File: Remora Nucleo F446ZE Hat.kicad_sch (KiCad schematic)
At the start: 20 parts, among them J1 NucleoF446ZE CN11 Header, J2 MSD-1-A, J3 UART_TX, J4 NucleoF446ZE CN12 Header, SW1 SW_Push

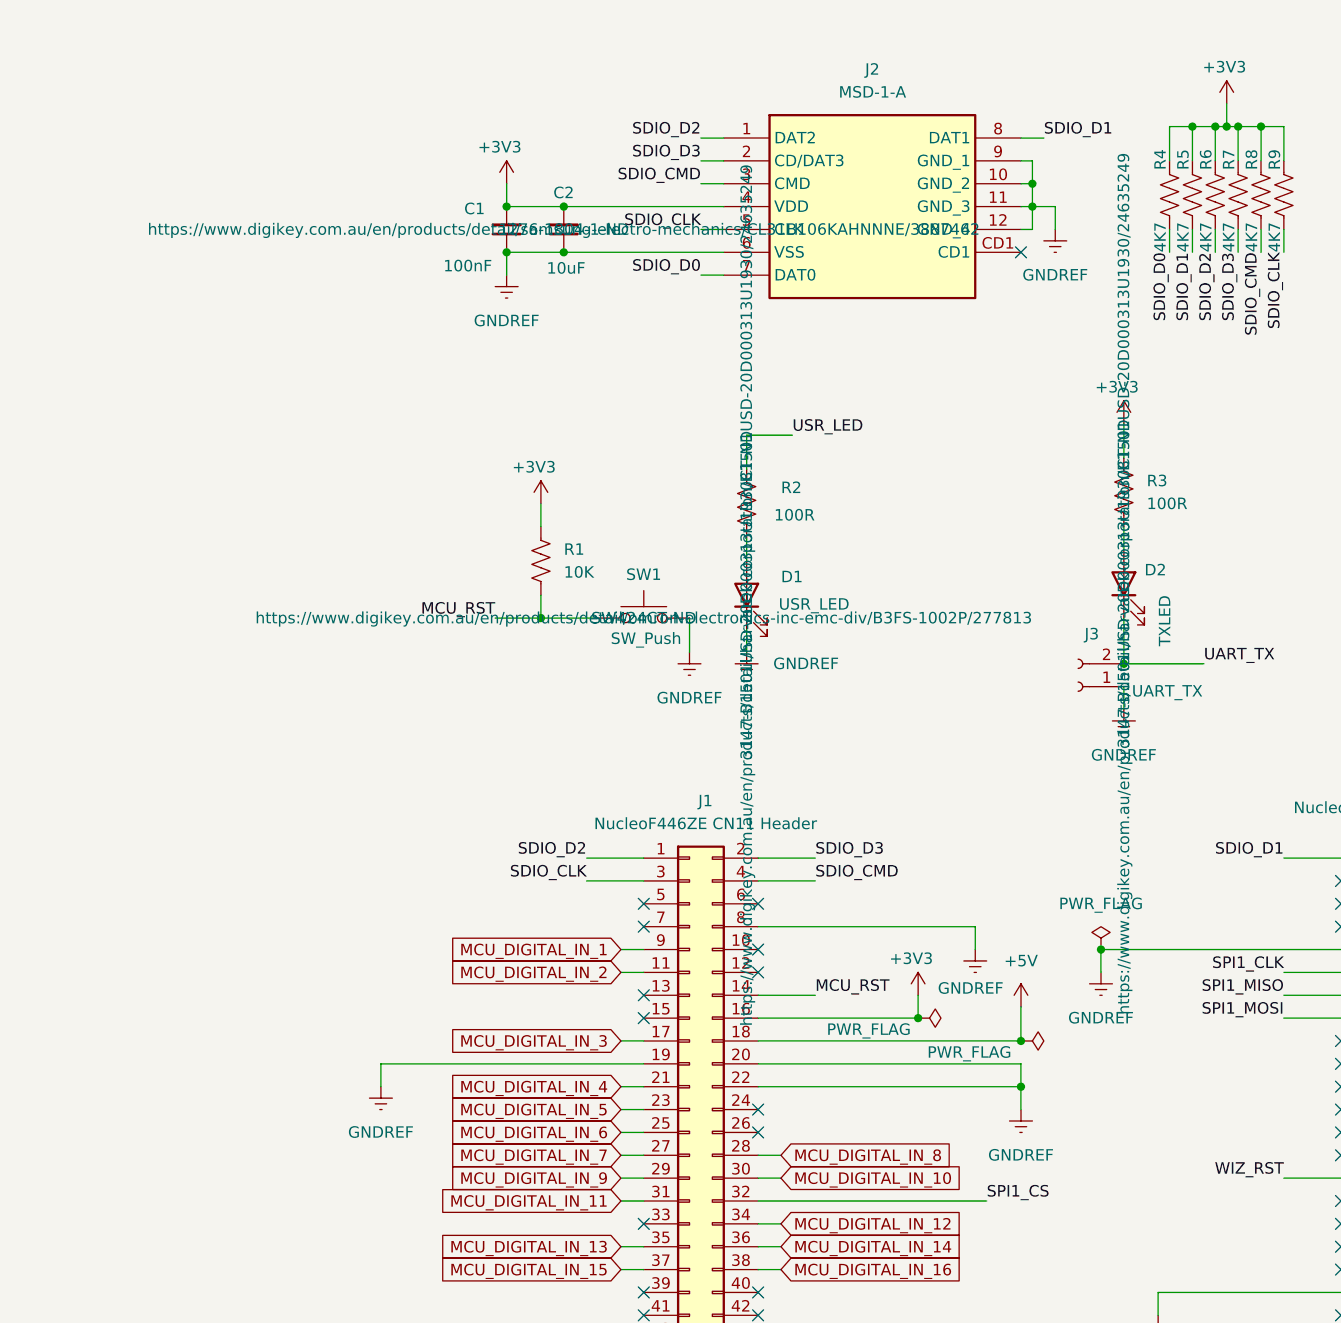
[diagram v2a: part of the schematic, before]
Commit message: fix to annoying additional symbol fields displaying when we didn't want them to.
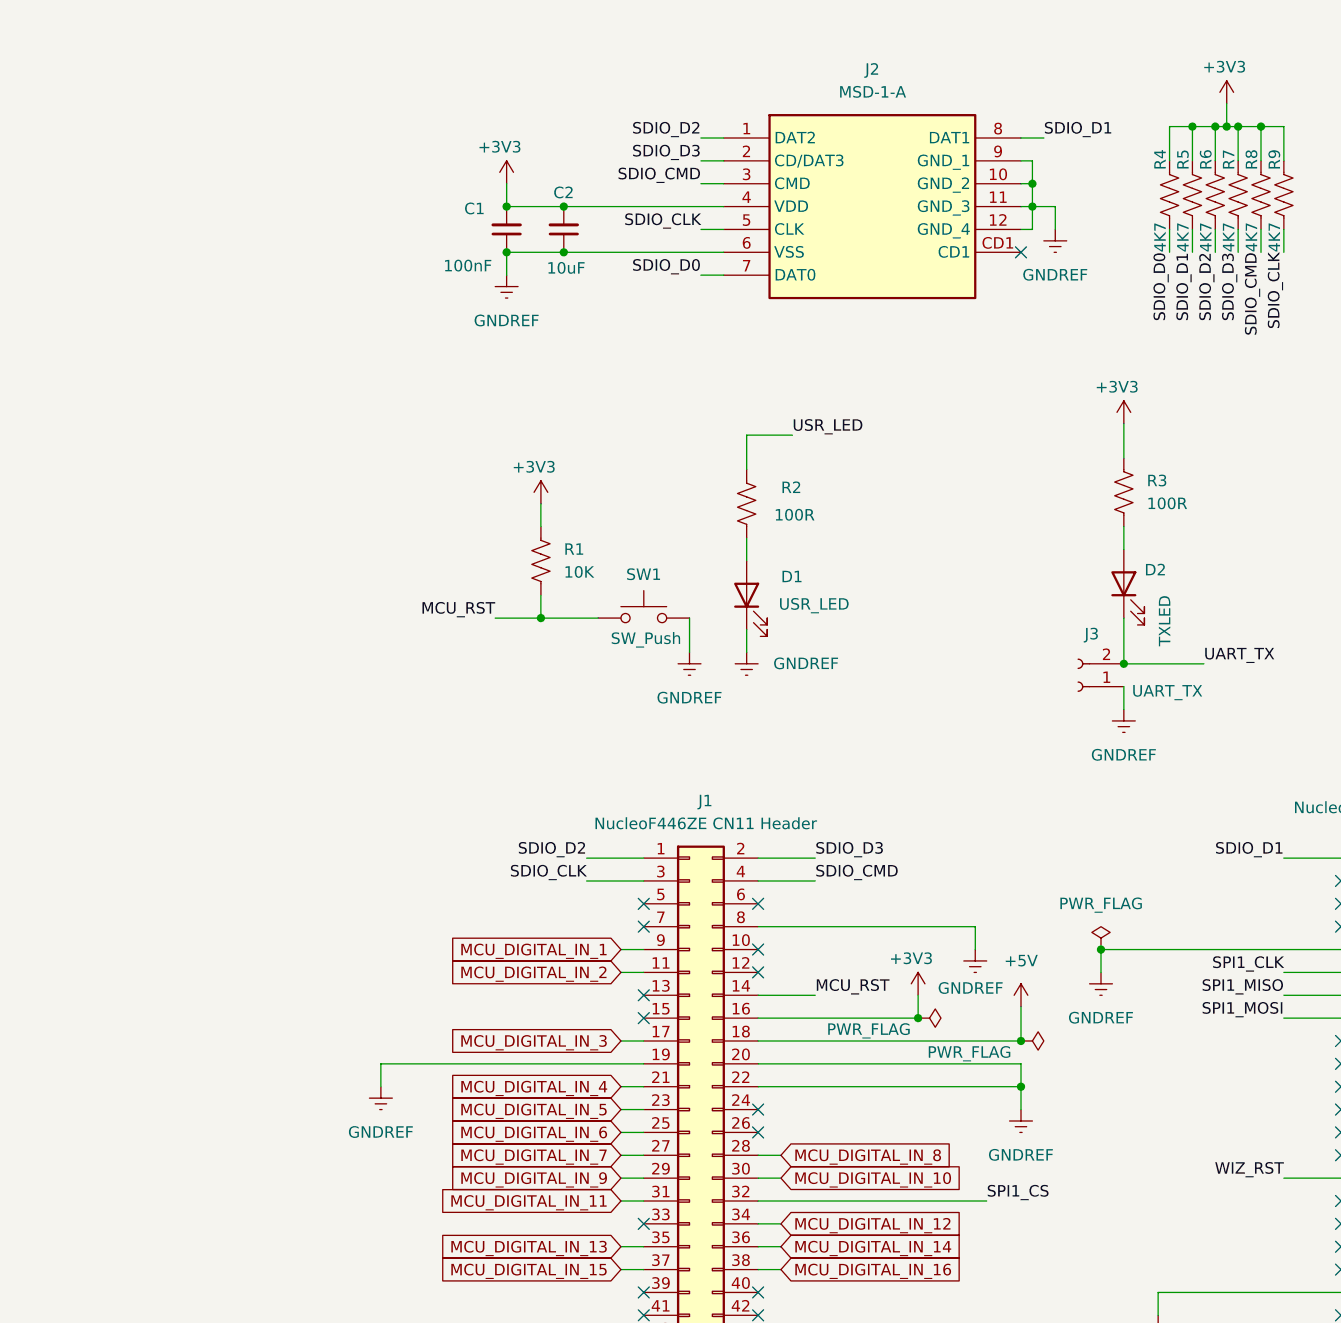
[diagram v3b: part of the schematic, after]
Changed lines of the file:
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@@
 					(size 1.27 1.27)
 				)
+				(hide yes)
 			)
 		)
@@
 					(size 1.27 1.27)
 				)
+				(hide yes)
 			)
 		)
@@
 					(size 1.27 1.27)
 				)
+				(hide yes)
 			)
 		)
@@
 					(size 1.27 1.27)
 				)
+				(hide yes)
 			)
 		)
@@
 					(size 1.27 1.27)
 				)
+				(hide yes)
 			)
 		)
@@
 					(size 1.27 1.27)
 				)
+				(hide yes)
 			)
 		)
@@
 					(size 1.27 1.27)
 				)
+				(hide yes)
 			)
 		)
@@
 					(size 1.27 1.27)
 				)
+				(hide yes)
 			)
 		)
@@
 					(size 1.27 1.27)
 				)
+				(hide yes)
 			)
 		)
@@
 					(size 1.27 1.27)
 				)
+				(hide yes)
 			)
 		)
@@
 					(size 1.27 1.27)
 				)
+				(hide yes)
 			)
 		)
@@
 					(size 1.27 1.27)
 				)
+				(hide yes)
 			)
 		)
@@
 					(size 1.27 1.27)
 				)
+				(hide yes)
 			)
 		)
@@
 					(size 1.27 1.27)
 				)
+				(hide yes)
 			)
 		)
@@
 					(size 1.27 1.27)
 				)
+				(hide yes)
 			)
 		)
@@
 					(size 1.27 1.27)
 				)
+				(hide yes)
 			)
 		)
@@
 					(size 1.27 1.27)
 				)
+				(hide yes)
 			)
 		)
@@
 					(size 1.27 1.27)
 				)
+				(hide yes)
 			)
 		)
@@
 					(size 1.27 1.27)
 				)
+				(hide yes)
 			)
 		)
@@
 					(size 1.27 1.27)
 				)
+				(hide yes)
 			)
 		)
@@
 					(size 1.27 1.27)
 				)
+				(hide yes)
 			)
 		)
@@
 					(size 1.27 1.27)
 				)
+				(hide yes)
 			)
 		)
@@
 					(size 1.27 1.27)
 				)
+				(hide yes)
 			)
 		)
@@
 					(size 1.27 1.27)
 				)
+				(hide yes)
 			)
 		)
@@
 					(size 1.27 1.27)
 				)
+				(hide yes)
 			)
 		)
@@
 					(size 1.27 1.27)
 				)
+				(hide yes)
 			)
 		)
@@
 					(size 1.27 1.27)
 				)
+				(hide yes)
 			)
 		)
@@
 					(size 1.27 1.27)
 				)
+				(hide yes)
 			)
 		)
@@
 					(size 1.27 1.27)
 				)
+				(hide yes)
 			)
 		)
@@
 					(size 1.27 1.27)
 				)
+				(hide yes)
 			)
 		)
@@
 					(size 1.27 1.27)
 				)
+				(hide yes)
 			)
 		)
@@
 					(size 1.27 1.27)
 				)
+				(hide yes)
 			)
 		)
@@
 					(size 1.27 1.27)
 				)
+				(hide yes)
 			)
 		)
@@
 					(size 1.27 1.27)
 				)
+				(hide yes)
 			)
 		)
@@
 					(size 1.27 1.27)
 				)
+				(hide yes)
 			)
 		)
@@
 					(size 1.27 1.27)
 				)
+				(hide yes)
 			)
 		)

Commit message: BOM consolidation for various resistors. Moved BOM into symbol libraries and updated supplimentary BOM. Switched IO optical isolation circuitry to a more cost effective part.
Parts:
- removed R1: 10K, Resistor_SMD:R_1206_3216Metric_Pad1.30x1.75mm_HandSolder, symbol Device:R_US
- removed R2, R3: 100R, Resistor_SMD:R_1206_3216Metric_Pad1.30x1.75mm_HandSolder, symbol Device:R_US
- added R44: 4K7, Resistor_SMD:R_1206_3216Metric_Pad1.30x1.75mm_HandSolder, symbol Device:R_US
- added R53, R54: 180R, Resistor_SMD:R_1206_3216Metric_Pad1.30x1.75mm_HandSolder, symbol Device:R_US
- J1, J4: Digikey Part Number (none) -> SSW-135-03-T-D-ND; Digikey URL (none) -> https://www.digikey.com.au/en/products/detail/samtec-inc/SS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
- J2: Digikey Part Number (none) -> 2223-MSD-1-ACT-ND; Digikey URL (none) -> https://www.digikey.com.au/en/products/detail/same-sky-form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
- J3: Digikey Part Number (none) -> PH1-02-UA; Digikey URL (none) -> https://www.digikey.com.au/en/products/detail/adam-tech/PH1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
- R4, R5, R6, R7, R8, R9: Digikey Part Number (none) -> 311-4.70KFRCT-ND; Digikey URL (none) -> https://www.digikey.com.au/en/products/detail/yageo/RC1206F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
- RP1: Digikey Part Number (none) -> SAM15594-ND; Digikey URL (none) -> https://www.digikey.com.au/en/products/detail/samtec-inc/ES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
- U1: Digikey Part Number (none) -> SAM12520-ND; Digikey URL (none) -> https://www.digikey.com.au/en/products/detail/samtec-inc/ES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
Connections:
- net +3V3: now also R44.1, R54.1
- net MCU_RST: now also R44.2
- net USR_LED: now also R53.1
- net at D2.2 (A): now also R54.2
- net at D1.2 (A): now also R53.2
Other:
- sheet Inputs renamed Digital Inputs

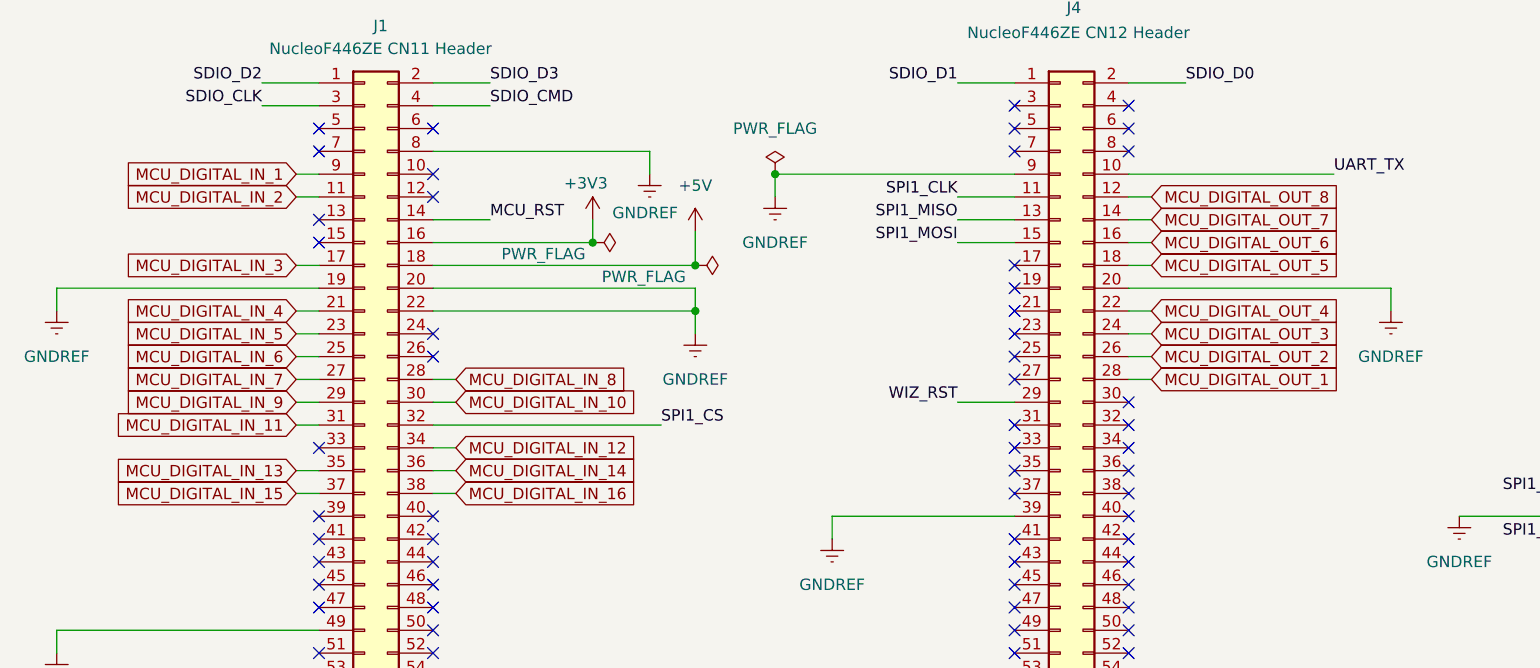
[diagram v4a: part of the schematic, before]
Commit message: Renumbered IO to start at 0 to match firmware
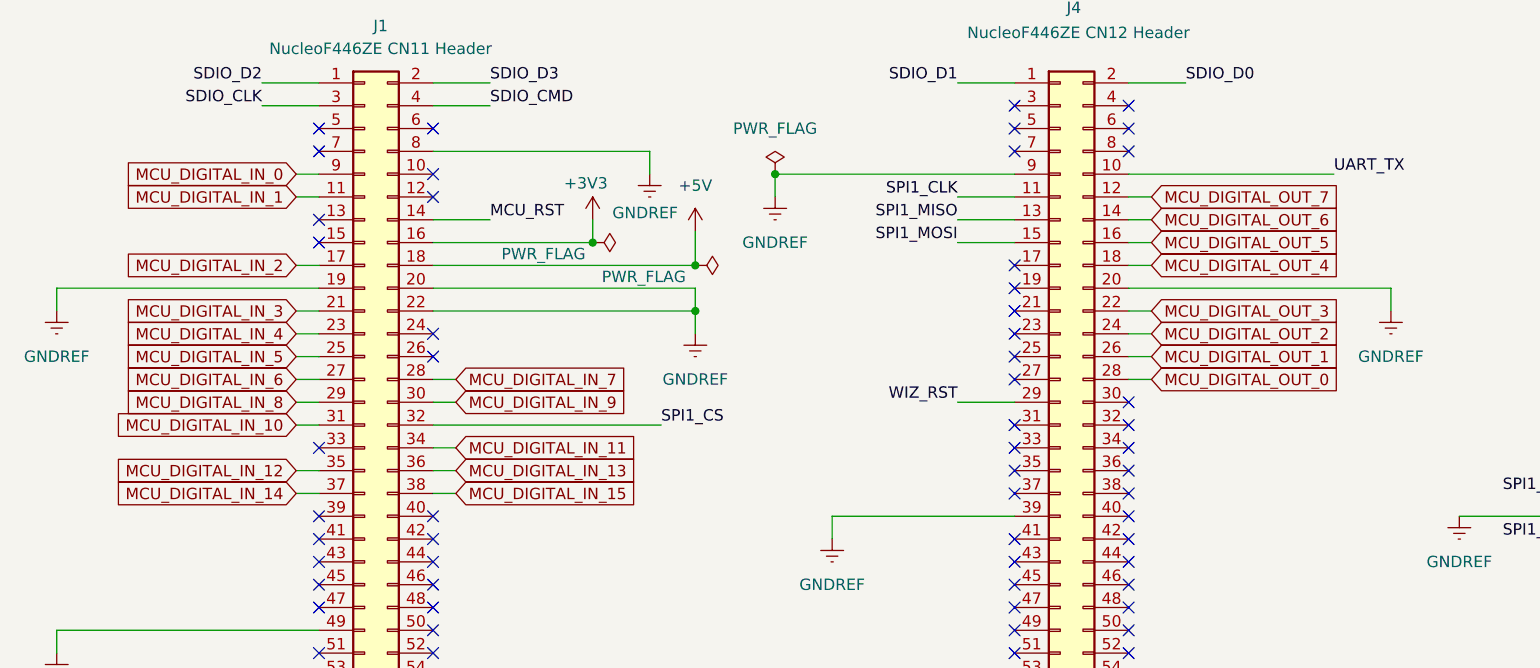
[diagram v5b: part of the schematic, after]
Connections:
- net MCU_DIGITAL_IN_16 is gone; now on net MCU_DIGITAL_IN_15: J1.38 (Pin_38)
- net MCU_DIGITAL_OUT_8 is gone; now on net MCU_DIGITAL_OUT_7: J4.12 (Pin_12)
- net MCU_DIGITAL_IN_1: now also J1.11 (Pin_11); no longer J1.9 (Pin_9)
- net MCU_DIGITAL_IN_10: now also J1.31 (Pin_31); no longer J1.30 (Pin_30)
- net MCU_DIGITAL_IN_11: now also J1.34 (Pin_34); no longer J1.31 (Pin_31)
- net MCU_DIGITAL_IN_12: now also J1.35 (Pin_35); no longer J1.34 (Pin_34)
- net MCU_DIGITAL_IN_13: now also J1.36 (Pin_36); no longer J1.35 (Pin_35)
- net MCU_DIGITAL_IN_14: now also J1.37 (Pin_37); no longer J1.36 (Pin_36)
- net MCU_DIGITAL_IN_15: no longer J1.37 (Pin_37)
- net MCU_DIGITAL_IN_2: now also J1.17 (Pin_17); no longer J1.11 (Pin_11)
- net MCU_DIGITAL_IN_3: now also J1.21 (Pin_21); no longer J1.17 (Pin_17)
- net MCU_DIGITAL_IN_4: now also J1.23 (Pin_23); no longer J1.21 (Pin_21)
- net MCU_DIGITAL_IN_5: now also J1.25 (Pin_25); no longer J1.23 (Pin_23)
- net MCU_DIGITAL_IN_6: now also J1.27 (Pin_27); no longer J1.25 (Pin_25)
- net MCU_DIGITAL_IN_7: now also J1.28 (Pin_28); no longer J1.27 (Pin_27)
- net MCU_DIGITAL_IN_8: now also J1.29 (Pin_29); no longer J1.28 (Pin_28)
- net MCU_DIGITAL_IN_9: now also J1.30 (Pin_30); no longer J1.29 (Pin_29)
- net MCU_DIGITAL_OUT_1: now also J4.26 (Pin_26); no longer J4.28 (Pin_28)
- net MCU_DIGITAL_OUT_2: now also J4.24 (Pin_24); no longer J4.26 (Pin_26)
- net MCU_DIGITAL_OUT_3: now also J4.22 (Pin_22); no longer J4.24 (Pin_24)
- net MCU_DIGITAL_OUT_4: now also J4.18 (Pin_18); no longer J4.22 (Pin_22)
- net MCU_DIGITAL_OUT_5: now also J4.16 (Pin_16); no longer J4.18 (Pin_18)
- net MCU_DIGITAL_OUT_6: now also J4.14 (Pin_14); no longer J4.16 (Pin_16)
- net MCU_DIGITAL_OUT_7: no longer J4.14 (Pin_14)
- new net MCU_DIGITAL_IN_0: J1.9 (Pin_9)
- new net MCU_DIGITAL_OUT_0: J4.28 (Pin_28)

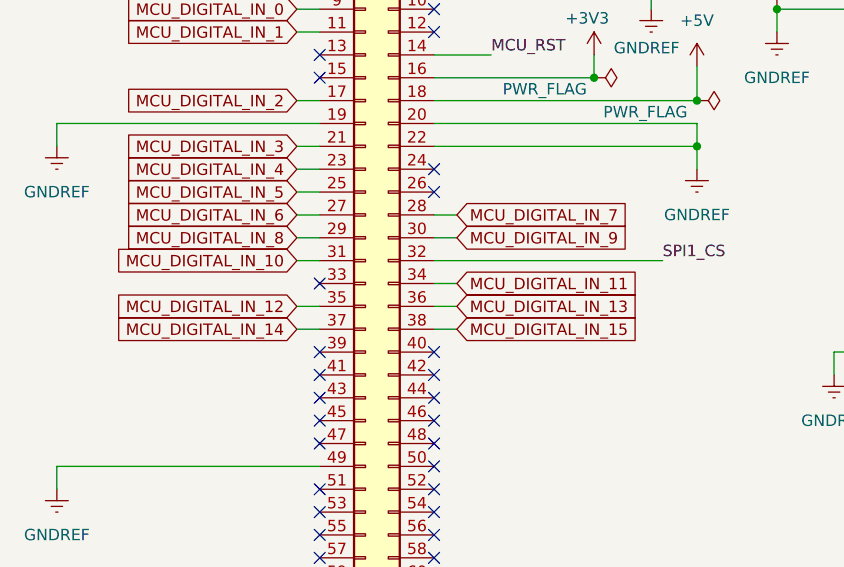
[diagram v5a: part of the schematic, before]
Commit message: Corrections to digital input pins
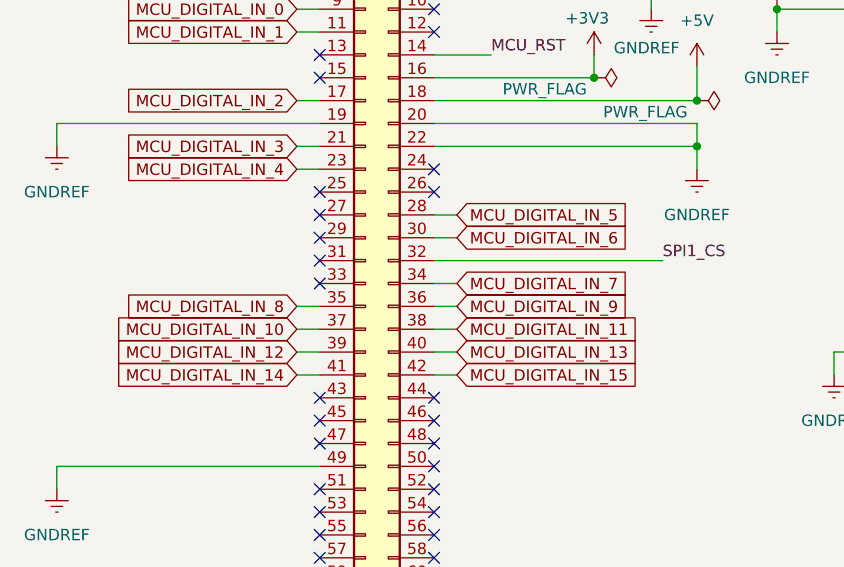
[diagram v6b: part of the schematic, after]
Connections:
- net MCU_DIGITAL_IN_10: now also J1.37 (Pin_37); no longer J1.31 (Pin_31)
- net MCU_DIGITAL_IN_11: now also J1.38 (Pin_38); no longer J1.34 (Pin_34)
- net MCU_DIGITAL_IN_12: now also J1.39 (Pin_39); no longer J1.35 (Pin_35)
- net MCU_DIGITAL_IN_13: now also J1.40 (Pin_40); no longer J1.36 (Pin_36)
- net MCU_DIGITAL_IN_14: now also J1.41 (Pin_41); no longer J1.37 (Pin_37)
- net MCU_DIGITAL_IN_15: now also J1.42 (Pin_42); no longer J1.38 (Pin_38)
- net MCU_DIGITAL_IN_5: now also J1.28 (Pin_28); no longer J1.25 (Pin_25)
- net MCU_DIGITAL_IN_6: now also J1.30 (Pin_30); no longer J1.27 (Pin_27)
- net MCU_DIGITAL_IN_7: now also J1.34 (Pin_34); no longer J1.28 (Pin_28)
- net MCU_DIGITAL_IN_8: now also J1.35 (Pin_35); no longer J1.29 (Pin_29)
- net MCU_DIGITAL_IN_9: now also J1.36 (Pin_36); no longer J1.30 (Pin_30)
